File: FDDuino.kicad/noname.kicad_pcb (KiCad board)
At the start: 2 copper layers, 7 parts, among them P1 RASPI_V2, P3 LS04, P5 LS04, P7 MSX_SLOT, U1 74LS74, U2 7400, U3 74F676

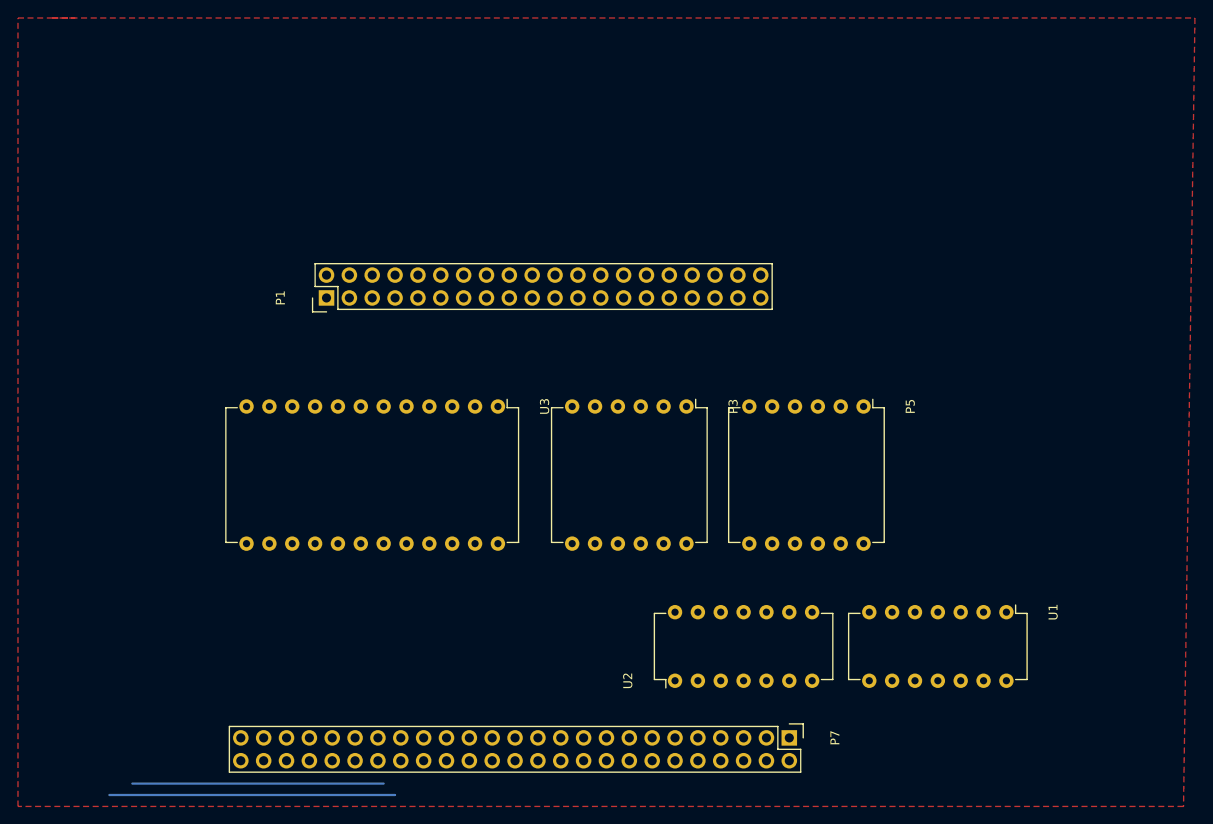
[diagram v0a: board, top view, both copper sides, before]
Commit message: FDDuino schematic update for correcting PIN number in Raspberry Pi GPIO
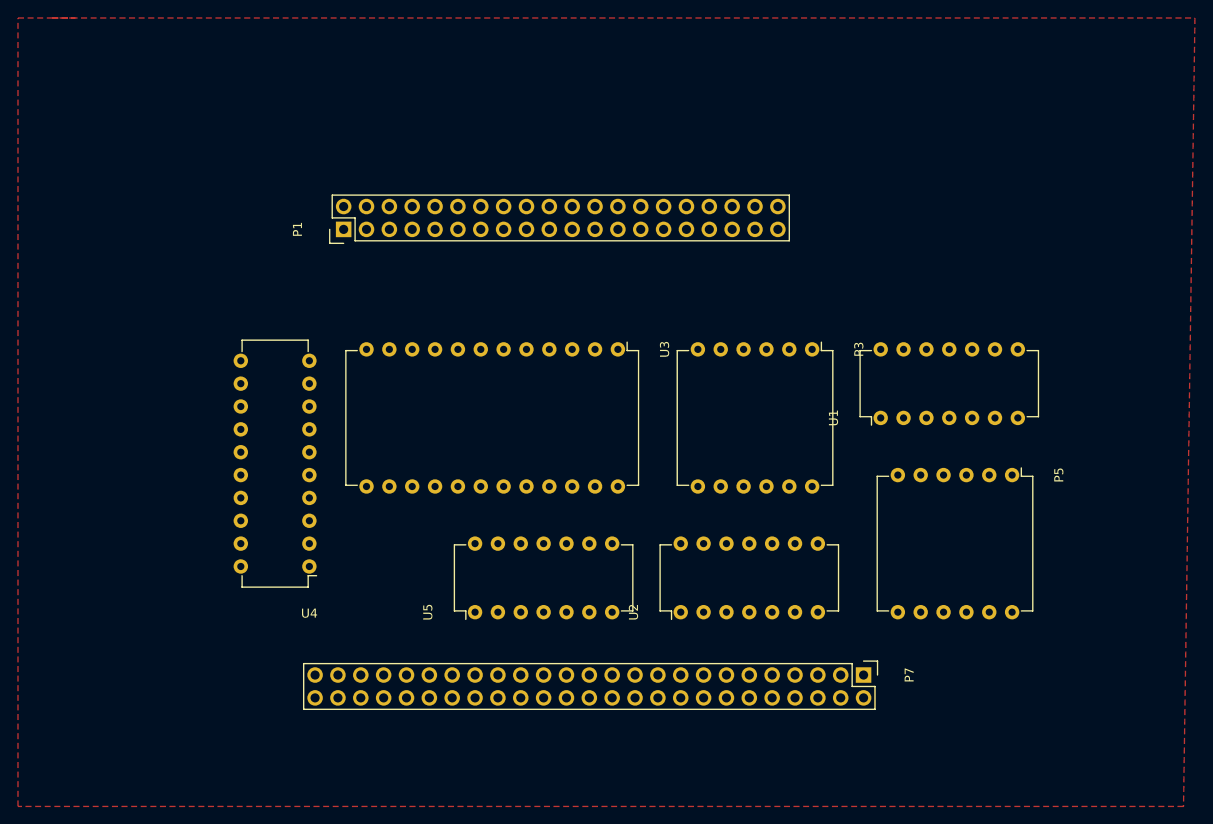
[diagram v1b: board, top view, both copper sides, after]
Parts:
- added U4: 74LS245, Housings_DIP:DIP-20_W7.62mm, F.Cu at (127.6, 120.7)
- added U5: 74LS00, Housings_DIP:DIP-14_W7.62mm, F.Cu at (146.1, 125.7)
- moved U1 25.7 mm to (191.1, 104.1), turned to 90 degrees
- moved P5 18.2 mm to (205.7, 110.5)
- moved P3 15.3 mm to (183.5, 96.5)
- moved U3 14.8 mm to (161.9, 96.5)
- moved P7 10.8 mm to (189.2, 132.7)
- moved P1 7.85 mm to (131.4, 83.2)
- moved U2 7.65 mm to (168.9, 125.7)
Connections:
- net G21 renamed /WR
- P1 pad 10: G12 -> G15
- P1 pad 32: G15 -> G12
- P1 pad 33: G14 -> G13
- P1 pad 8: G13 -> G14
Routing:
- net (no net): track 59.7 -> 0.00 mm
